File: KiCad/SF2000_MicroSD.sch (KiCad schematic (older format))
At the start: 1 part, among them J6 Micro_SD_Card_Socket

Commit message: added buffering for IDE, rearranged components a bit and did more routing
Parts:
- J6: footprint (none) -> SF2000:GCT-MEM2055-00-190-01-A
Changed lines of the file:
@@
 F 0 "J6" H 5650 4317 50  0000 C CNN
 F 1 "Micro_SD_Card_Socket" H 5650 4226 50  0000 C CNN
-F 2 "" H 6850 3900 50  0001 C CNN
+F 2 "SF2000:GCT-MEM2055-00-190-01-A" H 6850 3900 50  0001 C CNN
 F 3 "" H 5700 3600 50  0001 C CNN
 	1    5700 3600

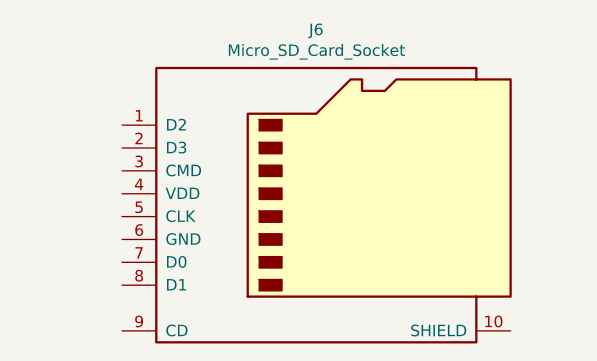
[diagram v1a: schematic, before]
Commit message: Added SDIO-pinout and did more routing
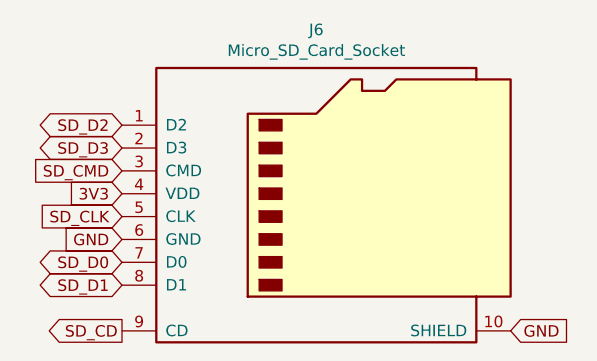
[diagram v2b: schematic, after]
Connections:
- net SD_D2: now reaches J6.1 (D2)
- net GND: now reaches J6.10 (SHIELD)
- net GND: now also J6.6 (GND)
- net SD_D3: now reaches J6.2 (D3)
- net SD_CMD: now reaches J6.3 (CMD)
- net 3V3: now reaches J6.4 (VDD)
- net SD_CLK: now reaches J6.5 (CLK)
- net SD_D0: now reaches J6.7 (D0)
- net SD_D1: now reaches J6.8 (D1)
- net SD_CD: now reaches J6.9 (CD)
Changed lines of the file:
@@
 	1    0    0    -1
 $EndComp
+Text GLabel 4800 3900 0    50   BiDi ~ 0
+SD_D0
+Text GLabel 4800 4000 0    50   BiDi ~ 0
+SD_D1
+Text GLabel 4800 3300 0    50   BiDi ~ 0
+SD_D2
+Text GLabel 4800 3400 0    50   BiDi ~ 0
+SD_D3
+Text GLabel 4800 3500 0    50   Input ~ 0
+SD_CMD
+Text GLabel 4800 3600 0    50   Input ~ 0
+3V3
+Text GLabel 4800 3800 0    50   Input ~ 0
+GND
+Text GLabel 6500 4200 2    50   Input ~ 0
+GND
+Text GLabel 4800 3700 0    50   Input ~ 0
+SD_CLK
+Text GLabel 4800 4200 0    50   Output ~ 0
+SD_CD
 $EndSCHEMATC

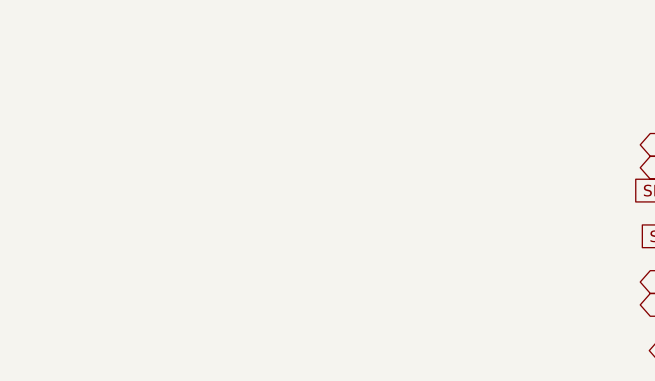
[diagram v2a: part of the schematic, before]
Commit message: added pull-ups for SDIO and did some more routing
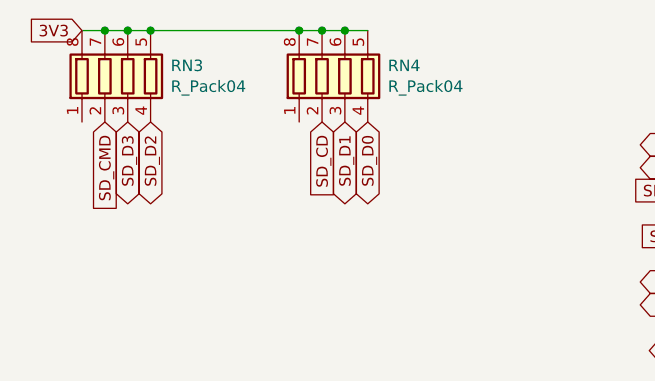
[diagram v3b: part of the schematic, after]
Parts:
- added RN3, RN4: R_Pack04, SF2000:RESCAF80P320X160X60-8N, symbol Device:R_Pack04
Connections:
- net 3V3: now also RN3.5 (R4.2), RN3.6 (R3.2), RN3.7 (R2.2), RN3.8 (R1.2), RN4.5 (R4.2), RN4.6 (R3.2), RN4.7 (R2.2), RN4.8 (R1.2)
- net SD_CD: now also RN4.2 (R2.1)
- net SD_CMD: now also RN3.2 (R2.1)
- net SD_D0: now also RN4.4 (R4.1)
- net SD_D1: now also RN4.3 (R3.1)
- net SD_D2: now also RN3.4 (R4.1)
- net SD_D3: now also RN3.3 (R3.1)
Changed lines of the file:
@@
 Text GLabel 4800 4200 0    50   Output ~ 0
 SD_CD
+$Comp
+L Device:R_Pack04 RN3
+U 1 1 61FDB219
+P 2200 3000
+F 0 "RN3" H 2388 3046 50  0000 L CNN
+F 1 "R_Pack04" H 2388 2955 50  0000 L CNN
+F 2 "SF2000:RESCAF80P320X160X60-8N" V 2475 3000 50  0001 C CNN
+F 3 "~" H 2200 3000 50  0001 C CNN
+	1    2200 3000
+	1    0    0    -1
+$EndComp
+$Comp
+L Device:R_Pack04 RN4
+U 1 1 61FDC27F
+P 3150 3000
+F 0 "RN4" H 3338 3046 50  0000 L CNN
+F 1 "R_Pack04" H 3338 2955 50  0000 L CNN
+F 2 "SF2000:RESCAF80P320X160X60-8N" V 3425 3000 50  0001 C CNN
+F 3 "~" H 3150 3000 50  0001 C CNN
+	1    3150 3000
+	1    0    0    -1
+$EndComp
+Text GLabel 2000 2800 0    50   Input ~ 0
+3V3
+Wire Wire Line
+	2000 2800 2100 2800
+Connection ~ 2100 2800
+Wire Wire Line
+	2100 2800 2200 2800
+Connection ~ 2200 2800
+Wire Wire Line
+	2200 2800 2300 2800
+Connection ~ 2300 2800
+Wire Wire Line
+	2300 2800 2950 2800
+Connection ~ 2950 2800
+Wire Wire Line
+	2950 2800 3050 2800
+Connection ~ 3050 2800
+Wire Wire Line
+	3050 2800 3150 2800
+Connection ~ 3150 2800
+Wire Wire Line
+	3150 2800 3250 2800
+Text GLabel 2300 3200 3    50   BiDi ~ 0
+SD_D2
+Text GLabel 2200 3200 3    50   BiDi ~ 0
+SD_D3
+Text GLabel 2100 3200 3    50   Input ~ 0
+SD_CMD
+Text GLabel 3250 3200 3    50   BiDi ~ 0
+SD_D0
+Text GLabel 3150 3200 3    50   BiDi ~ 0
+SD_D1
+Text GLabel 3050 3200 3    50   Input ~ 0
+SD_CD
 $EndSCHEMATC

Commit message: more routing and pin assignments done to FPGA
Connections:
- net FLASH_BUSY: now reaches RN3.1 (R1.1)
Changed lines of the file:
@@
 Text GLabel 3050 3200 3    50   Input ~ 0
 SD_CD
+Text GLabel 2000 3200 3    50   Input ~ 0
+FLASH_BUSY
 $EndSCHEMATC

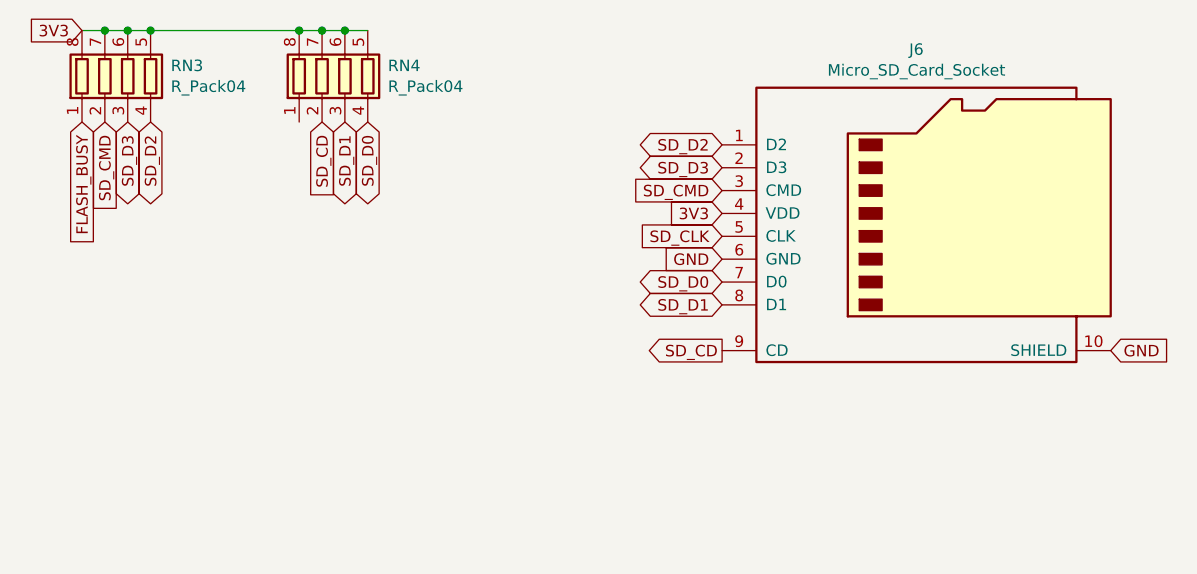
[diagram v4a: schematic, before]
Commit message: added Oscillator, pull-up resistor and more routing done
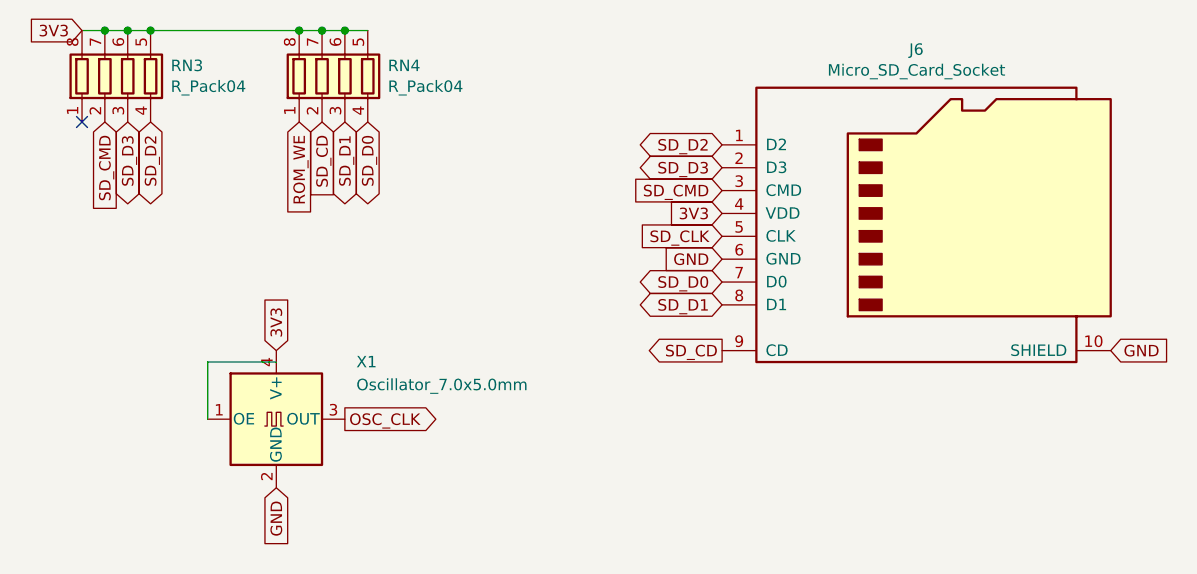
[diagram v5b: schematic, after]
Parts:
- added X1: Oscillator_7.0x5.0mm, Oscillator:Oscillator_SMD_SeikoEpson_SG8002CA-4Pin_7.0x5.0mm, symbol Oscillator:SG-8002CA
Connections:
- net labels added: OSC_CLK, ROM_WE
- net labels removed: FLASH_BUSY
- wire segments 7 -> 9
- no-connect marks 0 -> 1
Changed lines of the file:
@@
 Text GLabel 3050 3200 3    50   Input ~ 0
 SD_CD
-Text GLabel 2000 3200 3    50   Input ~ 0
-FLASH_BUSY
+$Comp
+L Oscillator:SG-8002CA X1
+U 1 1 620EE0AB
+P 2850 4500
+F 0 "X1" H 3200 4750 50  0000 L CNN
+F 1 "Oscillator_7.0x5.0mm" H 3200 4650 50  0000 L CNN
+F 2 "Oscillator:Oscillator_SMD_SeikoEpson_SG8002CA-4Pin_7.0x5.0mm" H 3550 4150 50  0001 C CNN
+F 3 "" H 2750 4500 50  0001 C CNN
+	1    2850 4500
+	1    0    0    -1
+$EndComp
+Text GLabel 2850 4200 1    50   Input ~ 0
+3V3
+Text GLabel 2850 4800 3    50   Input ~ 0
+GND
+Wire Wire Line
+	2850 4250 2550 4250
+Wire Wire Line
+	2550 4250 2550 4500
+Text GLabel 3150 4500 2    50   Output ~ 0
+OSC_CLK
+Text GLabel 2950 3200 3    50   Input ~ 0
+ROM_WE
+NoConn ~ 2000 3200
 $EndSCHEMATC

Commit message: more routing and fixing of FPGA pin assignments
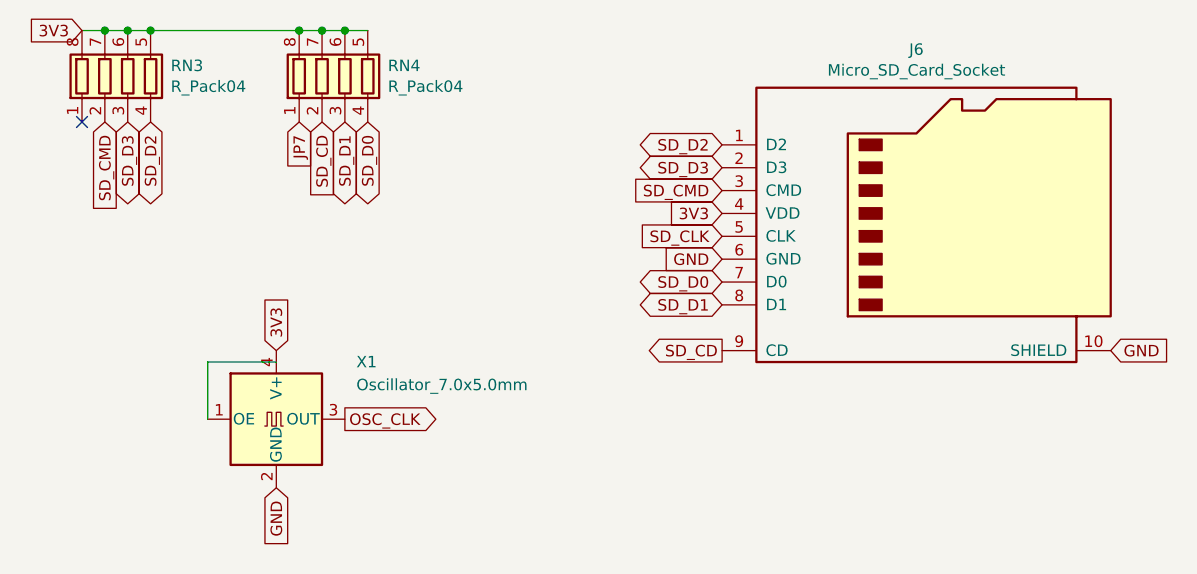
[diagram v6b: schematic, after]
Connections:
- net labels added: JP7
- net labels removed: ROM_WE
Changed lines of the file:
@@
 Text GLabel 3150 4500 2    50   Output ~ 0
 OSC_CLK
+NoConn ~ 2000 3200
 Text GLabel 2950 3200 3    50   Input ~ 0
-ROM_WE
-NoConn ~ 2000 3200
+JP7
 $EndSCHEMATC

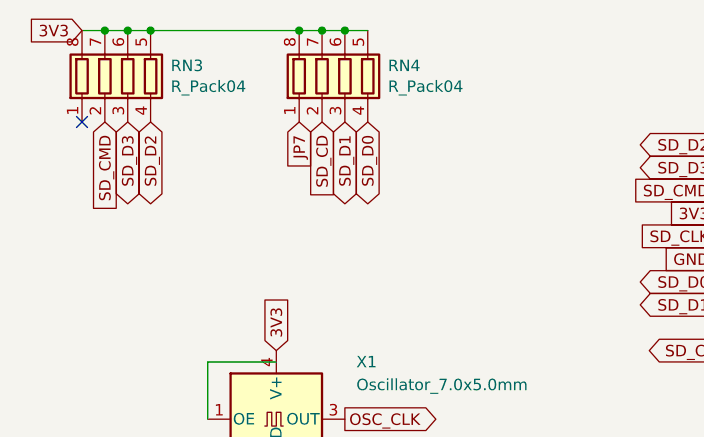
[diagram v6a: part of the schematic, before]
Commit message: Fixed Switch and Jumper enumeration and silkscreen
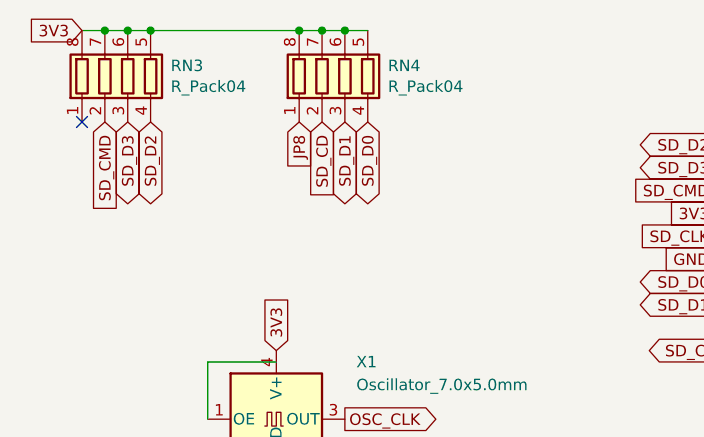
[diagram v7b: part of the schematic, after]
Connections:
- net labels added: JP8
- net labels removed: JP7
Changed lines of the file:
@@
 NoConn ~ 2000 3200
 Text GLabel 2950 3200 3    50   Input ~ 0
-JP7
+JP8
 $EndSCHEMATC

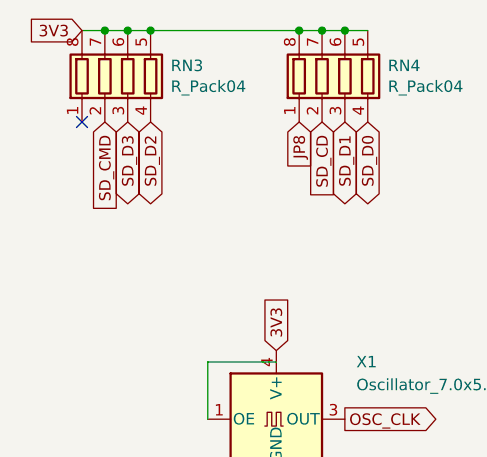
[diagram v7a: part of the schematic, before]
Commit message: added ROM_WE signal/pin to FPGA, removed XRDY-signal/pin, and some silkscreen fixes
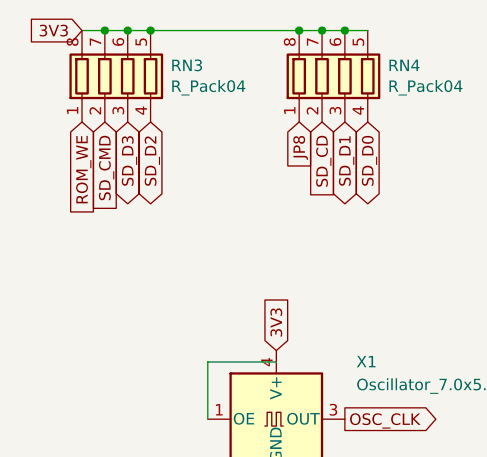
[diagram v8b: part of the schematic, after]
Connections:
- net labels added: ROM_WE
- no-connect marks 1 -> 0
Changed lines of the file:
@@
 Text GLabel 3150 4500 2    50   Output ~ 0
 OSC_CLK
-NoConn ~ 2000 3200
 Text GLabel 2950 3200 3    50   Input ~ 0
 JP8
+Text GLabel 2000 3200 3    50   Input ~ 0
+ROM_WE
 $EndSCHEMATC
